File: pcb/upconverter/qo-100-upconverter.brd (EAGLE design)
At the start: 90 x 55 mm, 153 parts, among them CON1 2EDG-2P, U1 EFM32PG1B100F256GM32, U10 MIC23155, U11 LT8636, U12 ADP3334, U13 ADP7142AUJZ-3.3, U14 ADP7142AUJZ-3.3, U15 ADP3334, U2 ADF4351, U3 F1951NBGI, U4 MAX2671, U5 2450BP15E0100, U6 ADL5601, U7 ADL5601, U8 F1951NBGI, U9 ADL5606

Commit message: Work on Upconverter
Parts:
- removed JP1: PINHD-1X3, Pin Header:1X03
- added C82: 10uF, Capacitor:CAP0603
- added C83: 1nF, Capacitor:CAP0603
- added C84: 470pF, Capacitor:CAP0603
- added C85: 10uF, Capacitor:CAP1206
- added CON2: 2EDG-2P-5MM, Generic Connector:2EDG-2P-5MM
- added D6: LED0603, LED:0603
- added R36: 210K Ohms, Resistor:RES0603
- added R37: 64.9K Ohms, Resistor:RES0603
- added R38: 510 Ohms, Resistor:RES0603
- added R39: 330 Ohms, Resistor:RES0603
- added U16: ADP7142AUJZ-3.3, Analog Devices:SOT23-5
- added U17: ADP3334, Analog Devices:LFCSP8_3X3
- added U18: ADM7171ACPZ-5.0, Analog Devices:LFCSP8_3X3
- C10, C12, C14, C16, C67: value 100nF -> 10pF
- C11, C13, C15: value 10pF -> 100nF
- C17: value 10pF -> 0.7pF
- C19: value 0.7pF -> 15pF
- C20: value 15pF -> 39nF
- C21: value 39nF -> 2.7nF
- C22: value 2.7nF -> 1.2nF
- C23: value 1.2nF -> 100nF
- C26: value 100nF -> 1uF
- C27: value 10uF -> 100nF
- C28: value 100nF -> 100pF
- C29: value 100pF -> 47pF
- C31: value 47pF -> 220pF
- C32: value 220pF -> 15pF
- C33: value 15pF -> 100uF; device Capacitor:CAP0603 -> Capacitor:CAP1206
- C34, C49: value 100uF -> 1uF; device Capacitor:CAP1206 -> Capacitor:CAP0603
- C35, C39: value 1uF -> 1nF
- C36, C40: value 1nF -> 15pF
- C38: value 15pF -> 1uF
- C42, C56: value 15pF -> 100nF
- C43, C52: value 100nF -> 15pF
- C44: value 15pF -> 10uF
- C45: value 10uF -> 10nF
- C46: value 10nF -> 100uF; device Capacitor:CAP0603 -> Capacitor:CAP1206
- C50, C64: value 1uF -> 10nF
- C51: value 3.3F -> 100pF
- C53: value 10nF -> 3.3F
- C54: value 100pF -> 15pF
- C55: value 15pF -> 4.7uF
- C57: value 4.7uF -> 470pF
- C58: value 100nF -> 470pF
- C59: value 1uF -> 4.7uF
- C60: value 4.7uF -> 1uF
- C63: value 470pF -> 1uF
- C65: value 10nF -> 100nF
- C66: value 470pF -> 100nF
- C68: value 10pF -> 1uF
- C73: value 1uF -> 100nF
- C74: value 470pF -> 22uF; device Capacitor:CAP0603 -> Capacitor:CAP1206
- C75: value 1uF -> 15pF
- C80: value 470pF -> 33nF
- C81: device Capacitor:CAP1206 -> Capacitor:CAP0603
- CON1: value 2EDG-2P -> 3P-SH-SIDE; device Generic Connector:2EDG-2P -> JST:SH-03-SIDE
- D4: value LED0603 -> SMAJ24A; device LED:0603 -> TVS:DO214AC
- D5: value SMAJ24A -> LED0603; device TVS:DO214AC -> LED:0603
- R10: value 61.9 Ohms -> DNP
- R11: value 680 Ohms -> 105 Ohms
- R12: value 105 Ohms -> 360 Ohms
- R13: value 100K Ohms -> 61.9 Ohms
- R14: value 100 Ohms -> 680 Ohms
- R15: value 100K Ohms -> 105 Ohms
- R16: value 510 Ohms -> 100K Ohms
- R17, R4, R5: value 100K Ohms -> 100 Ohms
- R18: value 100 Ohms -> 100K Ohms
- R2: value 10K Ohms -> 1K Ohms
- R20: value 147K Ohms -> 100K Ohms
- R21: value 21K Ohms -> 510 Ohms
- R22: value 41.2K Ohms -> 100K Ohms
- R23: value 100K Ohms -> 10K Ohms
- R25: value 309K Ohms -> 100K Ohms
- R26: value 71.5K Ohms -> 41.2K Ohms
- R27: value 1M Ohms -> 309K Ohms
- R28: value 226K Ohms -> 71.5K Ohms
- R29: value 510 Ohms -> 1M Ohms
- R3: value 330 Ohms -> 1K Ohms
- R30: value 100K Ohms -> 226K Ohms
- R31: value 210K Ohms -> 10K Ohms
- R32: value 64.9K Ohms -> 10K Ohms
- R33: value 100K Ohms -> 0.03 Ohms; device Resistor:RES0603 -> Resistor:RES1206
- R34: value 210K Ohms -> 100K Ohms
- R35: value 64.9K Ohms -> 100K Ohms
- R6: value 5.1K Ohms -> 330 Ohms
- R7: value DNP -> 100K Ohms
- R8: value 105 Ohms -> 100K Ohms
- R9: value 360 Ohms -> 5.1K Ohms
- U12: value ADP3334 -> MCP3421-A0; device Analog Devices:LFCSP8_3X3 -> Microchip:SOT23-6
- U13: value ADP7142AUJZ-3.3 -> MCP6C02-020; device Analog Devices:SOT23-5 -> Microchip:SOT23-6
- U14: value ADP7142AUJZ-3.3 -> TX-8010-EAW-1070-25M0000000; device Analog Devices:SOT23-5 -> Microchip:TCXO-5032
- U15: value ADP3334 -> ADP7142AUJZ-3.3; device Analog Devices:LFCSP8_3X3 -> Analog Devices:SOT23-5
- moved R18 206.3 mm to (81.5, 40.9), turned to 270 degrees
- moved C45 194.9 mm to (20.2, 54.1)
- moved C52 194.8 mm to (11.9, 45.0)
- moved C47 192.4 mm to (20.2, 52.4)
- moved C46 170.4 mm to (11.5, 36.4), turned to 270 degrees
- moved C54 169.6 mm to (8.50, 50.0), turned to 180 degrees
- moved C53 165.7 mm to (11.1, 50.8), turned to 90 degrees
- moved L8 157.3 mm to (11.1, 47.5), turned to 270 degrees
- moved C50 156.0 mm to (11.9, 41.6)
- moved R17 145.5 mm to (80.6, 38.4), turned to 180 degrees
- moved C49 142.7 mm to (11.9, 39.9)
- moved C43 125.8 mm to (23.6, 49.0), turned to 180 degrees
- moved C55 120.4 mm to (27.1, 7.50), turned to 180 degrees
- moved U15 109.2 mm to (55.8, 43.2)
- moved C80 104.2 mm to (71.8, 23.1), turned to 270 degrees
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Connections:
- removed net !PA_BIAS_EN: R30.1, R33.1, U1.17, U12.6, U15.6
- removed net 3V3_ANA_MIXER_ATT_CLEAN: C25.1, C27.1, C28.1, C30.1, C31.1, C43.1, C78.1, L5.2, U13.4, U13.5, U3.14, U4.5, U8.14
- removed net 3V3_ANA_PLL_CLEAN: C6.1, C7.1, C79.1, C8.1, C9.1, L1.1, L2.2, U14.4, U14.5, U2.10, U2.16, U2.17, U2.32, U2.6
- removed net IF_FREQ_SEL: C5.1, JP1.2, R2.2, U1.32
- removed net PA_DISABLE: R18.1
- removed net PLL_REF_DCC: C11.1
- new net !PA_STG1_BIAS_EN: R35.1, U1.20, U17.6
- new net 3V3_MIXER_CLEAN: C24.1, C26.1, C27.1, C29.1, C30.1, C81.1, L5.2, U15.4, U15.5, U3.14, U4.5
- new net 3V3_PLL_CLEAN: C5.1, C6.1, C7.1, C8.1, C82.1, L1.1, L2.2, U14.8, U14.9, U16.4, U16.5, U2.10, U2.16, U2.17, U2.32, U2.6
- new net 5V0_ISENSE: C74.1, C76.1, C77.1, C78.1, C79.1, R33.1, U13.4, U15.1, U15.3, U16.1, U16.3, U17.7, U17.8, U17.9, U18.7, U18.8
- new net 5V0_ISENSE_VN: C72.2, R32.1, U12.6
- new net 5V0_ISENSE_VP: C72.1, R31.1, U12.1
- new net I2C_SCL: R2.1, U1.28, U12.3
- new net I2C_SDA: R3.1, U1.29, U12.4
- new net N$11: CON1.2, R5.1
- new net N$13: D6.A, R39.1
- new net N$17: CON1.1, R4.1
- new net N$21: C10.1, C75.1, U14.6
- new net N$24: C80.1, U14.7
- new net PA_STG2_BIAS_EN: R34.2, U1.21, U18.5
- new net UART_RX: R4.2, U1.31
- new net UART_TX: R5.2, U1.32
- net !IF_ATT_CS: now also U1.4; no longer U1.24
- net !IF_ATT_RST: now also R16.2, U1.5; no longer R13.2
- net !MIXER_SHDN: now also R17.2, U1.10; no longer R14.2, U1.4
- net !PLL_MUTE: now also R8.2, U1.16; no longer R5.2, U1.15
- net !RF_ATT_CS: now also U1.17
- net !RF_ATT_RST: now also R20.2, U1.18; no longer R17.2
- net 3V3: now also C65.1, C9.1, R2.2, R27.2, R3.2, R35.2, U12.5; no longer C10.1, JP1.1, R25.2, R30.2, R33.2
- net 3V3_FB: now also R27.1, R28.2; no longer R25.1, R26.2
- net 3V3_SOFTSTART: now also C61.1; no longer C63.1
- net 5V0: now also C56.1, C59.1, C67.1, R24.2, R33.2, R38.2, U13.6; no longer C58.1, C60.1, C72.1, C75.1, C76.1, C77.1, R23.2, R27.2, U12.7, U12.8, U12.9, U13.1, U14.1, U14.3, U15.7, U15.8, U15.9
- net 5V0_BST: now also C66.2; no longer C67.2
- net 5V0_FB: now also C67.2, R29.1, R30.2; no longer C68.2, R27.1, R28.2
- net 5V0_INTVCC: now also C63.1; no longer C64.1
- net 5V0_PA_STG1_CLEAN: now also C33.1, C38.1, C42.1, C84.1, R19.2, R36.2, U17.1, U17.2, U8.14; no longer C37.1, C41.1, C74.1, R16.2, R31.2, U12.1, U12.2
- net 5V0_PA_STG2_CLEAN: now also C44.1, C51.1, C52.1, R21.2, U18.1, U18.2, U18.3; no longer C53.1, C54.1, C55.1, C80.1, R19.2, R34.2, U15.1, U15.2
- net 5V0_RT: now also R26.2; no longer R22.2
- net 5V0_SS: now also C64.1; no longer C65.1
- net 5V0_SW: now also C66.1; no longer C67.1
- net 5V0_VSENSE: now also C58.1, R24.1, R25.2, U1.23; no longer C66.1, R23.1, R24.2, U1.19
- net GND: now also C11.2, C18.2, C21.2, C24.2, C26.2, C33.2, C38.2, C42.2, C44.2, C56.2, C68.2, C74.2, C80.2, C82.2, C83.2, C85.2, CON1.3, CON2.P$1, D4.A, D5.C, D6.C, R11.1, R16.1, R18.1, R20.1, R23.1, R25.1, R30.1, R32.2, R34.1, R37.1, R7.1, U12.2, U13.5, U14.10, U14.4, U14.5, U15.2, U16.2, U17.5, U18.6, U18.9, U9.2; no longer C10.2, C17.2, C19.2, C23.2, C25.2, C31.2, C37.2, C41.2, C43.2, C54.2, C66.2, C72.2, CON1.P$1, D4.C, D5.A, JP1.3, R13.1, R17.1, R2.1, R21.1, R22.1, R24.1, R32.1, R35.1, R4.1, R5.1, R6.1, U12.5, U14.2, U15.5
- net IF_IN_DCC: now also C23.1; no longer C24.1
- net LED: now also R6.2, U1.30; no longer R3.2, U1.31
- net MIXER_LO: now also R13.1, R15.2; no longer R10.1, R12.2
- net N$1: now also C17.2, C19.1; no longer C18.2, C20.1
- net N$10: now also R31.2, U13.1; no longer C52.1, R18.2, U9.2
- net N$12: now also C32.2; no longer C33.2
- net N$14: now also C37.1; no longer C38.1
- net N$149: now also D5.A, R38.1; no longer D4.A, R29.1
- net N$15: now also C37.2; no longer C38.2
- net N$16: now also C41.1; no longer C42.1
- net N$18: now also C54.2; no longer C56.2
- net N$19: now also CON2.P$2; no longer CON1.P$2
- net N$2: now also C83.1, U18.4; no longer C80.2, R34.1, R35.2, U15.3
- net N$20: now also C84.2, R36.1, R37.2, U17.3; no longer C74.2, R31.1, R32.2, U12.3
- net N$23: now also R19.1; no longer R16.1
- net N$25: now also R6.1; no longer R3.1
- net N$26: now also C23.2; no longer C24.2
- net N$27: now also C25.2; no longer C26.2
- net N$28: now also C25.1; no longer C26.1
- net N$29: now also C19.2, R11.2, R13.2; no longer C20.2, R10.2, R8.2
- net N$3: now also R21.1; no longer R19.1
- net N$4: now also C28.1, R17.1, R18.2; no longer C29.1, R14.1, R15.2
- net N$5: now also C43.2; no longer C44.2
- net N$6: now also C31.1; no longer C32.1
- net N$67: now also C18.1; no longer C19.1
- net N$69: now also C17.1; no longer C18.1
- net N$8: now also C53.1, C54.1; no longer C51.1, C56.1
- net N$84: now also C20.2, R10.1, R12.2; no longer C21.2, R7.1, R9.2
- net N$88: now also R9.2; no longer R6.2
- net N$9: now also C43.1; no longer C44.1
- net PLL_CP_VOUT: now also C20.1, R14.2; no longer C22.1, R11.2
- net PLL_EN: now also R7.2, U1.11; no longer R4.2, U1.10
- net PLL_FASTLOCK_SW: now also R10.2; no longer R7.2
- net PLL_LE: now also U1.12; no longer U1.11
- net PLL_LOCK: now also R39.2; no longer U1.16
- net PLL_MUXOUT: now also U1.15; no longer U1.14
- net PLL_REF_ACC: now also C10.2; no longer C11.2
- net PLL_TEMP: now also C15.1; no longer C17.1
- net PLL_VCOM: now also C13.1; no longer C15.1
- net PLL_VREF: now also C11.1; no longer C13.1
- net PLL_VTUNE: now also C22.1, R14.1; no longer C23.1, R11.1
- net RF_ACC: now also C31.2; no longer C32.2
- net RF_ACC_FILT: now also C32.1; no longer C33.1
- net RF_ACC_PRE: now also C41.2; no longer C42.2
- net SPI_MOSI: now also U1.13; no longer U1.12
- net SPI_SCK: now also U1.14; no longer U1.13
- net VIN: now also C55.1, C60.1, C85.1, D4.C, R22.2; no longer C57.1, C59.1, C81.1, D5.C, R20.2
- net VIN_VSENSE: now also C57.1, R22.1, R23.2, U1.24; no longer C61.1, R20.1, R21.2, U1.21
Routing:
- net 5V0_ISENSE: track 0.00 -> 85.4 mm, vias 0 -> 4
- net 3V3_PLL_CLEAN: track 0.00 -> 66.7 mm, vias 0 -> 5
- net 3V3_ANA_PLL_CLEAN: track 50.4 -> 0.00 mm, vias 5 -> 0
- net SPI_MOSI: track 7.87 -> 56.8 mm, vias 1 -> 5
- net SPI_SCK: track 7.40 -> 55.9 mm, vias 1 -> 5
- net !IF_ATT_RST: track 0.00 -> 44.9 mm, vias 0 -> 2
- net !IF_ATT_CS: track 0.00 -> 44.5 mm, vias 0 -> 2
- net !MIXER_SHDN: track 0.00 -> 40.0 mm, vias 0 -> 2
- net 3V3_MIXER_CLEAN: track 0.00 -> 36.3 mm, vias 0 -> 2
- net UART_TX: track 0.00 -> 34.7 mm, vias 0 -> 2
- net VIN_VSENSE: track 38.1 -> 4.45 mm, vias 4 -> 1
- net 5V0_PA_STG1_CLEAN: track 0.00 -> 33.4 mm
- net UART_RX: track 0.00 -> 31.8 mm, vias 0 -> 2
- net !RESET: track 0.03 -> 31.1 mm, vias 0 -> 4
- net 5V0_PA_STG2_CLEAN: track 0.00 -> 28.1 mm, vias 0 -> 2
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- added copper zone on layer 1, net 5V0_ISENSE
- added copper zone on layer 1, net 5V0_PA_STG2_CLEAN

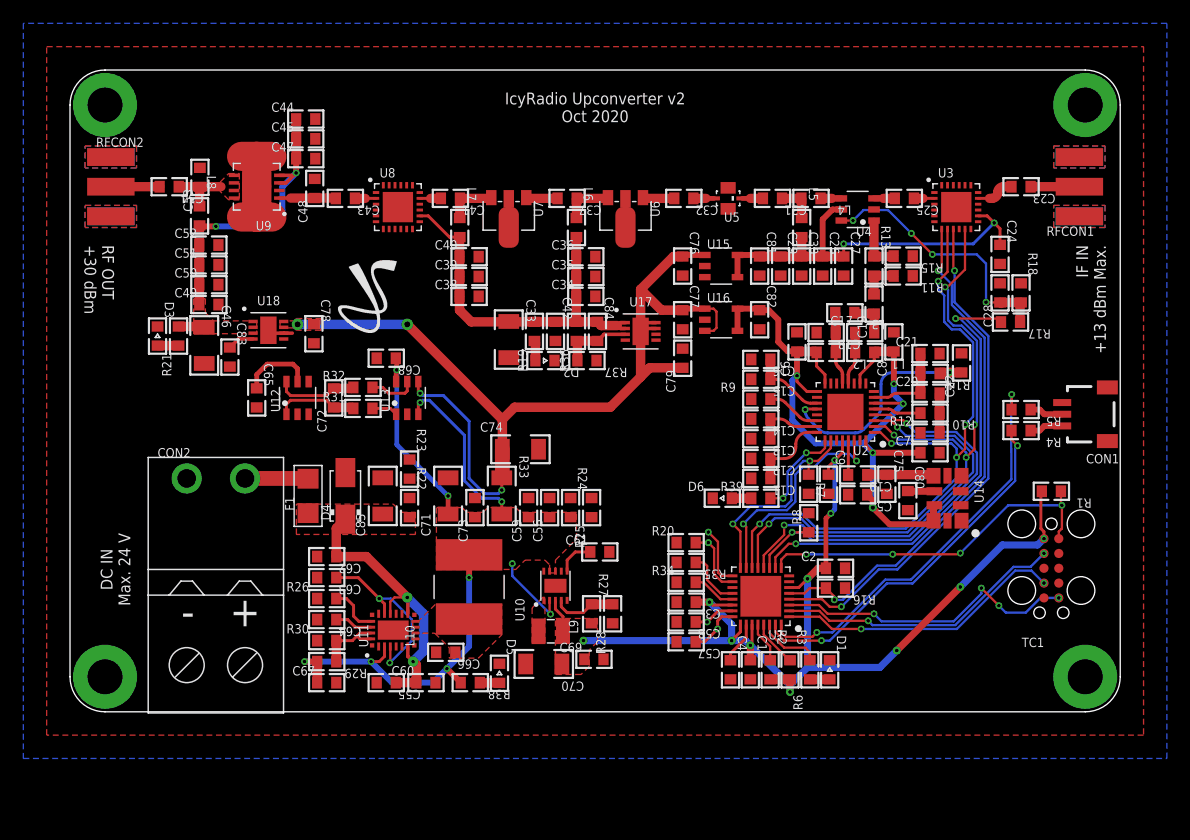
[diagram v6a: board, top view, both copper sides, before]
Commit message: Change Upconverter pre-amplifier
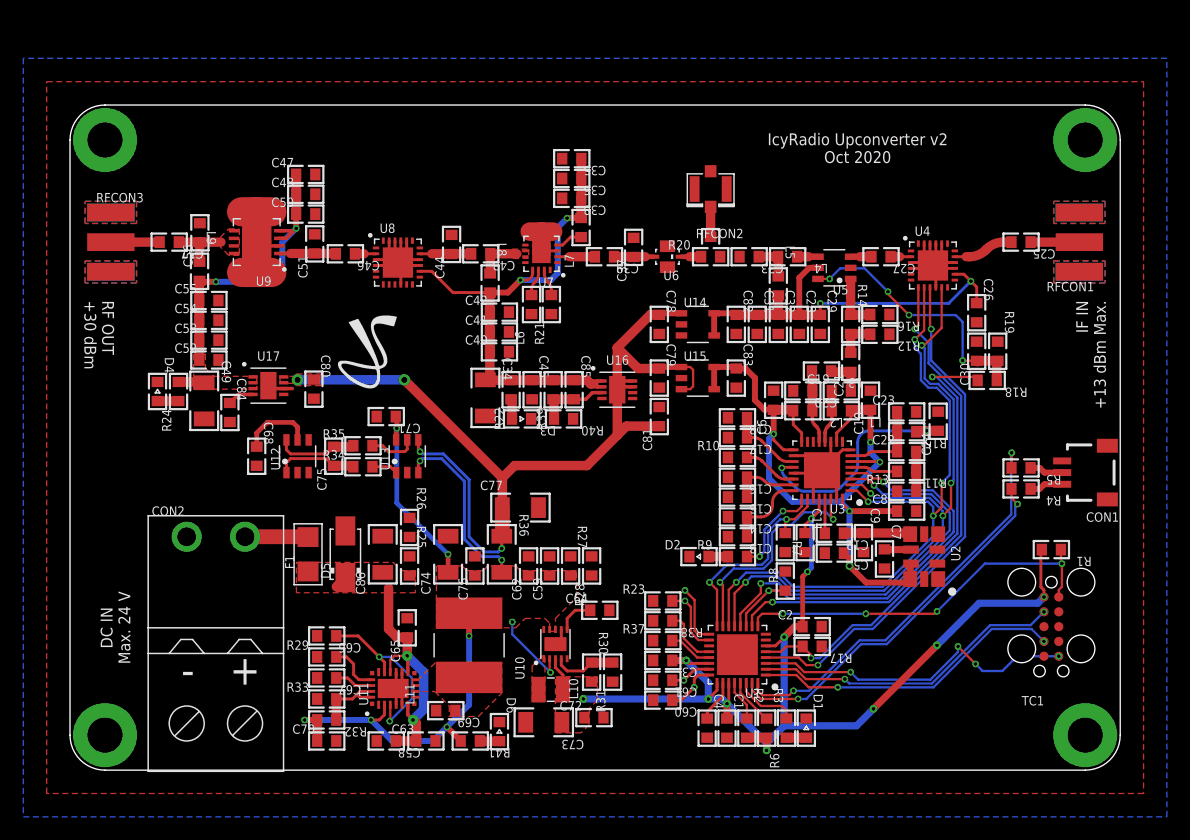
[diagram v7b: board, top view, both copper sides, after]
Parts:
- removed U18: ADM7171ACPZ-5.0, Analog Devices:LFCSP8_3X3
- added C86: 10uF, Capacitor:CAP1206
- added L11: 4.7uH, Inductor:IND0606
- added R40: 64.9K Ohms, Resistor:RES0603
- added R41: 510 Ohms, Resistor:RES0603
- added RFCON3: RFCON-SMA-EDGE, RF Connector:SMA-EDGE
- C10: value 10pF -> 100nF
- C17: value 0.7pF -> 100nF
- C18: value 0.7pF -> 10pF
- C19: value 15pF -> 0.7pF
- C20: value 39nF -> 0.7pF
- C21: value 2.7nF -> 15pF
- C22: value 1.2nF -> 39nF
- C23: value 100nF -> 2.7nF
- C24: value 100nF -> 1.2nF
- C26, C68, C76: value 1uF -> 100nF
- C28: value 100pF -> 1uF
- C29: value 47pF -> 100nF
- C30: value 47pF -> 100pF
- C31: value 220pF -> 47pF
- C32: value 15pF -> 47pF
- C33: value 100uF -> 220pF; device Capacitor:CAP1206 -> Capacitor:CAP0603
- C34, C49: value 1uF -> 100uF; device Capacitor:CAP0603 -> Capacitor:CAP1206
- C35: value 1nF -> 1uF
- C36, C41: value 15pF -> 1nF
- C37: value 15pF -> 0.5pF
- C38: value 1uF -> 15pF
- C39: value 1nF -> 100nF
- C40, C52: value 15pF -> 1uF
- C42, C9: value 100nF -> 15pF
- C43: value 15pF -> 10pF
- C44: value 10uF -> 1.2pF
- C45: value 10nF -> 100nF
- C46: value 100uF -> 15pF; device Capacitor:CAP1206 -> Capacitor:CAP0603
- C47: value 100pF -> 10uF
- C48: value 2pF -> 10nF
- C50: value 10nF -> 100pF
- C51: value 100pF -> 2pF
- C53: value 3.3F -> 10nF
- C54: value 15pF -> 100pF
- C55: value 4.7uF -> 15pF
- C56: value 100nF -> 3.3F
- C57: value 470pF -> 15pF
- C58: value 470pF -> 4.7uF
- C59: value 4.7uF -> 100nF
- C60: value 1uF -> 470pF
- C62: value 1uF -> 4.7uF
- C64: value 10nF -> 470pF
- C65, C66: value 100nF -> 1uF
- C67: value 10pF -> 10nF
- C7: value 100nF -> 33nF
- C70: value 100uF -> 10pF; device Capacitor:CAP1206 -> Capacitor:CAP0603
- C71: value 100uF -> 1uF; device Capacitor:CAP1206 -> Capacitor:CAP0603
- C73: value 100nF -> 100uF; device Capacitor:CAP0603 -> Capacitor:CAP1206
- C74: value 22uF -> 100uF
- C75: value 15pF -> 100nF
- C77: value 1uF -> 22uF; device Capacitor:CAP0603 -> Capacitor:CAP1206
- C80: value 33nF -> 1uF
- C81: value 10uF -> 1uF
- C83: value 1nF -> 10uF
- C84: value 470pF -> 1nF
- C85: value 10uF -> 470pF; device Capacitor:CAP1206 -> Capacitor:CAP0603
- D4: value SMAJ24A -> LED0603; device TVS:DO214AC -> LED:0603
- D5: value LED0603 -> SMAJ24A; device LED:0603 -> TVS:DO214AC
- L10: value 4.7uH -> 2.2uH; device Inductor:IND0606 -> Inductor:IND2520
- L6: value 470nH -> 3.9nH
- L7: value 470nH -> 3nH
- L8: value 47nH -> 62nH
- L9: value 2.2uH -> 62nH; device Inductor:IND2520 -> Inductor:IND0603
- R10: value DNP -> 5.1K Ohms
- R11: value 105 Ohms -> DNP
- R12: value 360 Ohms -> 105 Ohms
- R13: value 61.9 Ohms -> 360 Ohms
- R14: value 680 Ohms -> 61.9 Ohms
- R15: value 105 Ohms -> 680 Ohms
- R16: value 100K Ohms -> 105 Ohms
- R17: value 100 Ohms -> 100K Ohms
- R18: value 100K Ohms -> 100 Ohms
- R19, R38: value 510 Ohms -> 100K Ohms
- R20: value 100K Ohms -> 0 Ohms; device Resistor:RES0603 -> Resistor:RES0603-SEL
- R21: value 510 Ohms -> 10K Ohms
- R22, R24: value 100K Ohms -> 510 Ohms
- R23: value 10K Ohms -> 100K Ohms
- R26: value 41.2K Ohms -> 10K Ohms
- R27: value 309K Ohms -> 100K Ohms
- R28: value 71.5K Ohms -> 100K Ohms
- R29: value 1M Ohms -> 41.2K Ohms
- R30: value 226K Ohms -> 309K Ohms
- R31: value 10K Ohms -> 71.5K Ohms
- R32: value 10K Ohms -> 1M Ohms
- R33: value 0.03 Ohms -> 226K Ohms; device Resistor:RES1206 -> Resistor:RES0603
- R34, R35: value 100K Ohms -> 10K Ohms
- R36: value 210K Ohms -> 0.03 Ohms; device Resistor:RES0603 -> Resistor:RES1206
- R37: value 64.9K Ohms -> 100K Ohms
- R39: value 330 Ohms -> 210K Ohms
- R9: value 5.1K Ohms -> 330 Ohms
- RFCON2: value RFCON-SMA-EDGE -> RFCON-U.FL; device RF Connector:SMA-EDGE -> RF Connector:U.FL
- U14: value TX-8010-EAW-1070-25M0000000 -> ADP7142AUJZ-3.3; device Microchip:TCXO-5032 -> Analog Devices:SOT23-5
- U16: value ADP7142AUJZ-3.3 -> ADP3334; device Analog Devices:SOT23-5 -> Analog Devices:LFCSP8_3X3
- U17: value ADP3334 -> ADM7171ACPZ-5.0
- U2: value ADF4351 -> TX-8010-EAW-1070-25M0000000; device Analog Devices:QFN32 -> Microchip:TCXO-5032
- U3: value F1951NBGI -> ADF4351; device Renesas:QFN24 -> Analog Devices:QFN32
- U4: value MAX2671 -> F1951NBGI; device Maxim Integrated:SOT23-6 -> Renesas:QFN24
- U5: value 2450BP15E0100 -> MAX2671; device Generic Filter:2450BP15E0100 -> Maxim Integrated:SOT23-6
- U6: value ADL5601 -> 2450BP15E0100; device Analog Devices:SOT89 -> Generic Filter:2450BP15E0100
- U7: value ADL5601 -> F1478NLGA; device Analog Devices:SOT89 -> Renesas:QFN16
- moved C57 56.0 mm to (8.50, 45.2)
- moved C80 51.8 mm to (20.9, 32.6)
- moved RFCON2 51.4 mm to (54.9, 49.8)
- moved C75 47.5 mm to (22.6, 26.9), turned to 90 degrees
- moved C83 43.4 mm to (57.1, 33.6)
- moved L9 43.1 mm to (11.1, 42.8)
- moved R19 39.7 mm to (79.5, 35.9), turned to 270 degrees
- moved C56 38.1 mm to (11.1, 46.0)
- moved C55 36.1 mm to (11.9, 40.2), turned to 0 degrees
- moved C72 35.3 mm to (44.9, 4.50), turned to 0 degrees
- moved R24 35.0 mm to (9.30, 32.5), turned to 90 degrees
- moved R17 32.6 mm to (63.6, 10.6)
- moved C84 32.3 mm to (13.7, 30.6)
- moved U17 32.2 mm to (17.0, 33.0)
- moved R21 32.1 mm to (41.2, 39.9)
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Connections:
- new net N$30: C39.2, U7.2
- new net N$31: C33.2, R20.2
- new net N$32: R20.COM, RFCON2.P$3
- net !IF_ATT_CS: now also U4.9; no longer U3.9
- net !IF_ATT_RST: now also R17.2, U4.7; no longer R16.2, U3.7
- net !MIXER_SHDN: now also R18.2; no longer R17.2
- net !PA_STG1_BIAS_EN: now also R38.1, U16.6; no longer R35.1, U17.6
- net !PLL_MUTE: now also U3.26; no longer U2.26
- net !RF_ATT_RST: now also R23.2; no longer R20.2
- net 3V3: now also C11.1, C68.1, C72.1, C73.1, L10.2, R30.2, R38.2, U3.28; no longer C65.1, C69.1, C70.1, C9.1, L9.2, R27.2, R35.2, U2.28
- net 3V3_FB: now also R30.1, R31.2; no longer R27.1, R28.2
- net 3V3_MIXER_CLEAN: now also C28.1, C31.1, C32.1, C82.1, U14.4, U14.5, U4.14, U5.5; no longer C24.1, C27.1, C30.1, C81.1, U15.4, U15.5, U3.14, U4.5
- net 3V3_PLL_CLEAN: now also C10.1, C83.1, U15.4, U15.5, U2.8, U2.9, U3.10, U3.16, U3.17, U3.32, U3.6; no longer C7.1, C82.1, U14.8, U14.9, U16.4, U16.5, U2.10, U2.16, U2.17, U2.32, U2.6
- net 3V3_SOFTSTART: now also C64.1; no longer C61.1
- net 3V3_SW: now also L10.1; no longer L9.1
- net 5V0: now also C62.1, C70.1, C74.1, C76.1, L11.2, R27.2, R32.2, R36.2, R41.2; no longer C56.1, C67.1, C68.1, C73.1, L10.2, R24.2, R29.2, R33.2, R38.2
- net 5V0_BST: now also C69.2; no longer C66.2
- net 5V0_FB: now also C70.2, R32.1, R33.2; no longer C67.2, R29.1, R30.2
- net 5V0_INTVCC: now also C66.1; no longer C63.1
- net 5V0_ISENSE: now also C80.1, C81.1, R36.1, U14.1, U14.3, U16.7, U16.8, U16.9; no longer C74.1, C76.1, R33.1, U16.1, U16.3, U17.9, U18.7, U18.8
- net 5V0_ISENSE_VN: now also C75.2, R35.1; no longer C72.2, R32.1
- net 5V0_ISENSE_VP: now also C75.1, R34.1; no longer C72.1, R31.1
- net 5V0_PA_STG1_CLEAN: now also C41.1, C45.1, C85.1, L8.2, R22.2, R39.2, U16.1, U16.2, U7.13; no longer C33.1, C39.1, C84.1, L6.2, R19.2, R36.2, U17.1, U17.2
- net 5V0_PA_STG2_CLEAN: now also C48.1, C53.1, C54.1, C55.1, L9.2, R24.2, U17.1, U17.2, U17.3; no longer C44.1, C45.1, C46.1, C51.1, L8.2, R21.2, U18.1, U18.2, U18.3
- net 5V0_RT: now also R29.2; no longer R26.2
- net 5V0_SS: now also C67.1; no longer C64.1
- net 5V0_SW: now also C69.1, L11.1; no longer C66.1, L10.1
- net 5V0_VSENSE: now also C61.1, R27.1, R28.2; no longer C58.1, R24.1, R25.2
- net GND: now also C10.2, C17.2, C20.2, C23.2, C31.2, C32.2, C37.2, C41.2, C54.2, C66.2, C67.2, C72.2, C84.2, C86.2, D4.C, D5.A, L6.1, R10.1, R13.1, R17.1, R19.1, R21.1, R29.1, R31.1, R33.1, R35.2, R40.1, RFCON2.P$1, RFCON2.P$2, RFCON3.GND@0, RFCON3.GND@1, RFCON3.GND@2, RFCON3.GND@3, U14.2, U16.5, U17.6, U17.9, U2.10, U2.4, U2.5, U3.11, U3.18, U3.27, U3.31, U3.33, U3.8, U3.9, U4.1, U4.10, U4.12, U4.13, U4.15, U4.16, U4.18, U4.19, U4.20, U4.21, U4.22, U4.23, U4.24, U4.25, U4.3, U4.4, U4.6, U5.2, U6.1, U6.3, U7.1, U7.12, U7.17, U7.3, U7.5, U7.6, U7.7, U7.8, U7.9, U8.1, U8.10, U8.12, U8.13, U8.15, U8.18, U8.4, U8.6, U9.13, U9.14, U9.15, U9.16, U9.5, U9.6, U9.7, U9.8; no longer C12.2, C21.2, C22.2, C27.2, C33.2, C39.2, C46.2, C57.2, C69.2, C70.2, C75.2, C85.2, D4.A, D5.C, R11.1, R15.1, R18.1, R20.1, R25.1, R30.1, R32.2, R34.1, R9.1, RFCON2.GND@0, RFCON2.GND@1, RFCON2.GND@2, RFCON2.GND@3, U14.10, U14.4, U14.5, U16.2, U17.5, U18.6, U18.9, U2.11, U2.18, U2.21, U2.27, U2.31, U2.33, U2.8, U2.9, U3.16, U3.19, U3.20, U3.22, U3.23, U3.24, U3.25, U3.3, U4.2, U5.1, U5.3, U6.2, U6.4, U7.2, U7.4
- net IF_IN_DCC: now also C25.1; no longer C23.1
- net MIXER_LO: now also R14.1, R16.2, U5.1; no longer R13.1, R15.2, U4.1
- net N$1: now also C19.2, C21.1; no longer C17.2, C19.1
- net N$10: now also R34.2; no longer R31.2
- net N$12: now also L7.1, U7.4; no longer C32.2, U6.1
- net N$13: now also D2.A, R9.1; no longer D6.A, R39.1
- net N$14: now also C43.1, L8.1, U7.10, U7.11; no longer C37.1, L6.1, U6.3
- net N$149: now also D6.A, R41.1; no longer D5.A, R38.1
- net N$15: now also R21.2, U7.15; no longer C37.2, U7.1
- net N$16: now also L6.2, U7.14; no longer C41.1, L7.1, U7.3
- net N$18: now also C57.2, RFCON3.SIG; no longer C54.2, RFCON2.SIG
- net N$2: now also C84.1, U17.4; no longer C83.1, U18.4
- net N$20: now also C85.2, R39.1, R40.2, U16.3; no longer C84.2, R36.1, R37.2, U17.3
- net N$21: now also C12.1, C9.1, U2.6; no longer C10.1, C75.1, U14.6
- net N$23: now also D3.A, R22.1; no longer D2.A, R19.1
- net N$24: now also C7.1, U2.7; no longer C80.1, U14.7
- net N$26: now also C25.2, U4.17; no longer C23.2, U3.17
- net N$27: now also C27.2, U5.3; no longer C25.2, U4.3
- net N$28: now also C27.1, U4.2; no longer C25.1, U3.2
- net N$29: now also C21.2, R12.2, R14.2; no longer C19.2, R11.2, R13.2
- net N$3: now also D4.A, R24.1; no longer D3.A, R21.1
- net N$4: now also C30.1, R18.1, R19.2, U5.6; no longer C28.1, R17.1, R18.2, U4.6
- net N$5: now also C46.2, C51.1; no longer C43.2, C48.1
- net N$6: now also C33.1; no longer C31.1
- net N$67: now also C20.1, U3.13; no longer C18.1, U2.13
- net N$69: now also C19.1, U3.12; no longer C17.1, U2.12
- net N$7: now also U5.4; no longer U4.4
- net N$8: now also C56.1, C57.1, L9.1; no longer C53.1, C54.1, L8.1
- net N$84: now also C22.2, R11.1, R13.2; no longer C20.2, R10.1, R12.2
- net N$88: now also R10.2, U3.22; no longer R9.2, U2.22
- net N$9: now also C46.1; no longer C43.1
- net PA_STG2_BIAS_EN: now also R37.2, U17.5; no longer R34.2, U18.5
- net PLL_CP_VOUT: now also C22.1, C23.1, R15.2, U3.7; no longer C20.1, C21.1, R14.2, U2.7
- net PLL_EN: now also U3.4; no longer U2.4
- net PLL_FASTLOCK_SW: now also R11.2, U3.5; no longer R10.2, U2.5
- net PLL_LE: now also U3.3; no longer U2.3
- net PLL_LOCK: now also R9.2, U3.25; no longer R39.2, U2.25
- net PLL_MUXOUT: now also U3.30; no longer U2.30
- net PLL_REF_ACC: now also C12.2, U3.29; no longer C10.2, U2.29
- net PLL_TEMP: now also C17.1, C18.1, U3.19; no longer C15.1, C16.1, U2.19
- net PLL_VCOM: now also C15.1, C16.1, U3.23; no longer C13.1, C14.1, U2.23
- net PLL_VREF: now also C13.1, C14.1, U3.24; no longer C11.1, C12.1, U2.24
- net PLL_VTUNE: now also C24.1, R15.1, U3.20; no longer C22.1, R14.1, U2.20
- net RF_ACC: now also R20.1, U6.4; no longer C31.2, U5.4
- net RF_ACC_FILT: now also C37.1, C39.1, U6.2; no longer C32.1, U5.2
- net RF_ACC_PRE: now also C43.2, C44.1; no longer C41.2
- net SPI_MOSI: now also U3.2, U4.11; no longer U2.2, U3.11
- net SPI_SCK: now also U3.1, U4.8; no longer U2.1, U3.8
- net VIN: now also C58.1, C63.1, C65.1, C86.1, D5.C, R25.2; no longer C55.1, C60.1, C62.1, C85.1, D4.C, R22.2
- net VIN_VSENSE: now also C60.1, R25.1, R26.2; no longer C57.1, R22.1, R23.2
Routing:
- net GND: track 16.6 -> 84.7 mm
- net 5V0_PA_STG1_CLEAN: track 33.4 -> 45.0 mm, vias 0 -> 2
- net N$30: track 0.00 -> 3.21 mm
- net VIN: track 26.7 -> 23.8 mm
- net RF_ACC_PRE: track 1.81 -> 4.42 mm
- net N$32: track 0.00 -> 2.57 mm
- net N$16: track 4.40 -> 2.28 mm
- net SWO: track 26.5 -> 28.5 mm
- net SWDIO: track 24.9 -> 26.9 mm
- net SWCLK: track 24.8 -> 26.8 mm
- net !RESET: track 31.1 -> 33.1 mm
- net 5V0_ISENSE: track 85.4 -> 83.5 mm
- net N$26: track 3.27 -> 5.12 mm
- net RF_ACC_FILT: track 1.78 -> 3.40 mm
- net UART_RX: track 31.8 -> 32.6 mm
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- added copper zone on layer 1, net N$14
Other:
- board size 90 x 55 mm -> 90 x 57 mm

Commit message: Nothing to do on Upconverter
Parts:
- removed C7: 33nF, Capacitor:CAP0603
- added R42: 10K Ohms, Resistor:RES0603
- added R43: 0 Ohms, Resistor:RES0603
- added RFCON4: RFCON-U.FL, RF Connector:U.FL
- C22: value 39nF -> 68nF
- C24: value 1.2nF -> 910pF
- C9: value 15pF -> 10pF
- R13: value 360 Ohms -> 866 Ohms
- R15: value 680 Ohms -> 6.65K Ohms
- U2: value TX-8010-EAW-1070-25M0000000 -> DSB321SDA; device Microchip:TCXO-5032 -> Crystal:TCXO-3225
- moved C9 6.36 mm to (73.8, 16.9), turned to 0 degrees
- moved U2 3.63 mm to (69.6, 17.8), turned to 0 degrees
- moved C70 1.42 mm to (21.1, 3.60), turned to 90 degrees
- moved R32 1.14 mm to (22.9, 3.60), turned to 270 degrees
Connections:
- removed net N$24: C7.1, U2.7
- new net PLL_REF_DCC: C12.1, C9.1, R42.2, R43.1, U2.3
- net 3V3_PLL_CLEAN: now also U2.4; no longer U2.8, U2.9
- net GND: now also R42.1, RFCON4.P$1, RFCON4.P$2, U2.1, U2.2; no longer C7.2, U2.10, U2.4, U2.5
- net N$21: now also R43.2, RFCON4.P$3; no longer C12.1, C9.1, U2.6
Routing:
- net I2C_SDA: track 4.02 -> 78.3 mm, vias 0 -> 2
- net I2C_SCL: track 3.49 -> 69.5 mm, vias 0 -> 2
- net 3V3: track 99.6 -> 161.8 mm, vias 11 -> 14
- net PA_STG2_BIAS_EN: track 3.75 -> 49.5 mm, vias 0 -> 2
- net SPI_MOSI: track 56.8 -> 100.0 mm, vias 5 -> 6
- net SPI_SCK: track 55.9 -> 98.8 mm, vias 5 -> 6
- net !RF_ATT_RST: track 5.83 -> 45.0 mm, vias 1 -> 2
- net !RF_ATT_CS: track 5.17 -> 42.8 mm, vias 1 -> 2
- net VIN_VSENSE: track 4.45 -> 35.2 mm, vias 1 -> 2
- net !PA_STG1_BIAS_EN: track 4.95 -> 29.3 mm, vias 0 -> 4
- net 5V0_VSENSE: track 3.54 -> 20.1 mm, vias 1 -> 2
- net PLL_REF_DCC: track 0.00 -> 11.9 mm
- net GND: track 84.7 -> 90.9 mm, vias 4 -> 39
- net 3V3_PLL_CLEAN: track 66.7 -> 60.6 mm
- net 5V0_ISENSE: track 83.5 -> 87.5 mm
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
